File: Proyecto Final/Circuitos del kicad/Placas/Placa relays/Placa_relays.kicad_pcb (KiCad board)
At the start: 2 copper layers, 266.2 x 179.3 mm, 47 parts, among them J1 12v, J4 Conn_01x08, J5 Conn_01x08, J6 Conn_01x06, Q1 PN2222A, Q2 PN2222A, Q3 PN2222A, SW1 SW_Push, SW2 SW_Push, SW3 SW_Push, SW4 SW_Push, U1 LM7805, U2 ESP-12E, U3 ATmega328P-P, U4 LM1117-3.3, U5 BOB-12009, Y1 16MHz

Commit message: Cambios placa relays
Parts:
- removed C1, C2: 20pF, Capacitor_THT:C_Disc_D5.0mm_W2.5mm_P5.00mm
- removed C3: 330nF, Capacitor_THT:C_Disc_D5.0mm_W2.5mm_P5.00mm
- removed C4, C5: 100nF, Capacitor_THT:C_Disc_D5.0mm_W2.5mm_P5.00mm
- removed C6: 10uF, Capacitor_THT:C_Disc_D5.0mm_W2.5mm_P5.00mm
- removed Encoder/puls-arduino1: Conn_02x06_Odd_Even, ENCODER+PULS:ENCODER+PULS_arduino
- removed Encoder/puls2: Conn_02x06_Odd_Even, ENCODER+PULS:ENCODER+PULS
- removed Encoder1: Conn_01x05, Connector_PinHeader_2.54mm:PinHeader_1x05_P2.54mm_Vertical
- removed J4, J5: Conn_01x08, Connector_PinHeader_2.54mm:PinHeader_1x08_P2.54mm_Vertical
- removed J6: Conn_01x06, Connector_PinHeader_2.54mm:PinHeader_1x06_P2.54mm_Vertical
- removed R7, R8: 10k, Resistor_THT:R_Axial_DIN0204_L3.6mm_D1.6mm_P5.08mm_Horizontal
- removed RTC+LCD1: Conn_02x04_Odd_Even, Connector_PinHeader_2.54mm:PinHeader_2x04_P2.54mm_Vertical
- removed Relay+DS18B20+LVL_SENS1: Conn_02x05_Odd_Even_1, RELAY+DS18B20+LVLSENS:RELAY+DS18B20+LVLSENS
- removed Relay1: Conn_02x05_Odd_Even, RELAY+DS18B20+LVLSENS:ENCODER+PULS_PLACA_SALIDAS
- removed SW1, SW2, SW3, SW4: SW_Push, Button_Switch_THT:SW_PUSH-12mm
- removed U1: LM7805, Package_TO_SOT_THT:TO-220-3_Vertical
- removed U2: ESP-12E, ESP8266-12E_ESP-12E:XCVR_ESP8266-12E_ESP-12E
- removed U3: ATmega328P-P, Package_DIP:DIP-28_W7.62mm
- removed U4: LM1117-3.3, Package_TO_SOT_SMD:SOT-223
- removed U5: BOB-12009, Conversor_logico_nivel:CONV_BOB-12009
- removed Y1: 16MHz, Crystal:Crystal_HC49-4H_Vertical
- added D4: LED, LED_THT:LED_D5.0mm, F.Cu at (147.7, 120.2)
- added D5: LED, LED_THT:LED_D5.0mm, F.Cu at (148.0, 93.7)
- added D6: LED, LED_THT:LED_D5.0mm, F.Cu at (148.2, 67.4)
- J1: value 12v -> Conn_02x05_Odd_Even; footprint TerminalBlock:TerminalBlock_bornier-2_P5.08mm -> Connector_IDC:IDC-Header_2x05_P2.54mm_Vertical
- R1: value 4.7k -> 470
- R5, R6: value 10k -> 470
- moved Salidas_sensores1 104.1 mm to (187.3, 67.2)
- moved D3 102.0 mm to (148.5, 75.4)
- moved R5 101.9 mm to (137.2, 91.5), turned to 0 degrees
- moved Salida-3 100.1 mm to (187.3, 101.0)
- moved D2 99.6 mm to (148.6, 86.7)
- moved R3 99.4 mm to (125.8, 77.8)
- moved Q1 99.3 mm to (130.6, 76.5)
- moved Salida-2 98.8 mm to (187.3, 114.1)
- moved Relay-1 97.7 mm to (154.5, 125.6)
- moved Relay-2 97.7 mm to (154.5, 97.4)
- moved Relay-3 97.7 mm to (154.6, 69.2)
- moved Salida-1 97.7 mm to (187.3, 127.1)
- moved R4 97.2 mm to (125.7, 86.3)
- moved D1 96.3 mm to (148.5, 99.3)
- moved R2 95.5 mm to (126.1, 95.2)
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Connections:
- J1 pad 2: +12V -> GND
- R1 pad 1: Net-(R1-Pad1) -> Net-(D1-Pad2)
- R1 pad 2: +5V -> Net-(D4-Pad2)
- R5 pad 1: Net-(Encoder/puls2-Pad3) -> Net-(D2-Pad2)
- R5 pad 2: +5V -> Net-(D5-Pad2)
- R6 pad 1: Net-(Encoder/puls2-Pad5) -> Net-(D3-Pad2)
- R6 pad 2: +5V -> Net-(D6-Pad2)
- Salidas_sensores1 pad 2: Net-(Relay1-Pad7) -> Net-(Salidas_sensores1-Pad2)
- Salidas_sensores1 pad 3: Net-(Relay1-Pad5) -> Net-(Salidas_sensores1-Pad3)
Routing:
- net +5V: track 560.4 -> 132.0 mm
- net GND: track 250.2 -> 0.02 mm, vias 7 -> 0
- net Net-(Encoder/puls2-Pad4): track 158.0 -> 0.00 mm
- net Net-(Encoder/puls2-Pad6): track 152.8 -> 0.00 mm
- net Net-(Encoder/puls2-Pad8): track 148.0 -> 0.00 mm
- net Net-(Encoder/puls-arduino1-Pad7): track 147.8 -> 0.00 mm, vias 2 -> 0
- net Net-(Relay1-Pad7): track 139.5 -> 0.00 mm
- net Net-(Relay1-Pad5): track 135.8 -> 0.00 mm
- net Net-(Salidas_sensores1-Pad2): track 0.00 -> 127.7 mm
- net Net-(Salidas_sensores1-Pad3): track 0.00 -> 125.3 mm
- net Net-(J4-Pad1): track 99.4 -> 0.00 mm, vias 1 -> 0
- net Net-(Encoder/puls2-Pad9): track 48.4 -> 0.00 mm
- net Net-(Encoder/puls2-Pad3): track 47.5 -> 0.00 mm
- net Net-(C6-Pad1): track 46.7 -> 0.00 mm, vias 1 -> 0
- net Net-(Encoder/puls-arduino1-Pad5): track 44.2 -> 0.00 mm
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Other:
- board size 266.2 x 179.3 mm -> 89.9 x 85.7 mm
- board text added: "-"
- board text added: "L"
- board text added: "T"

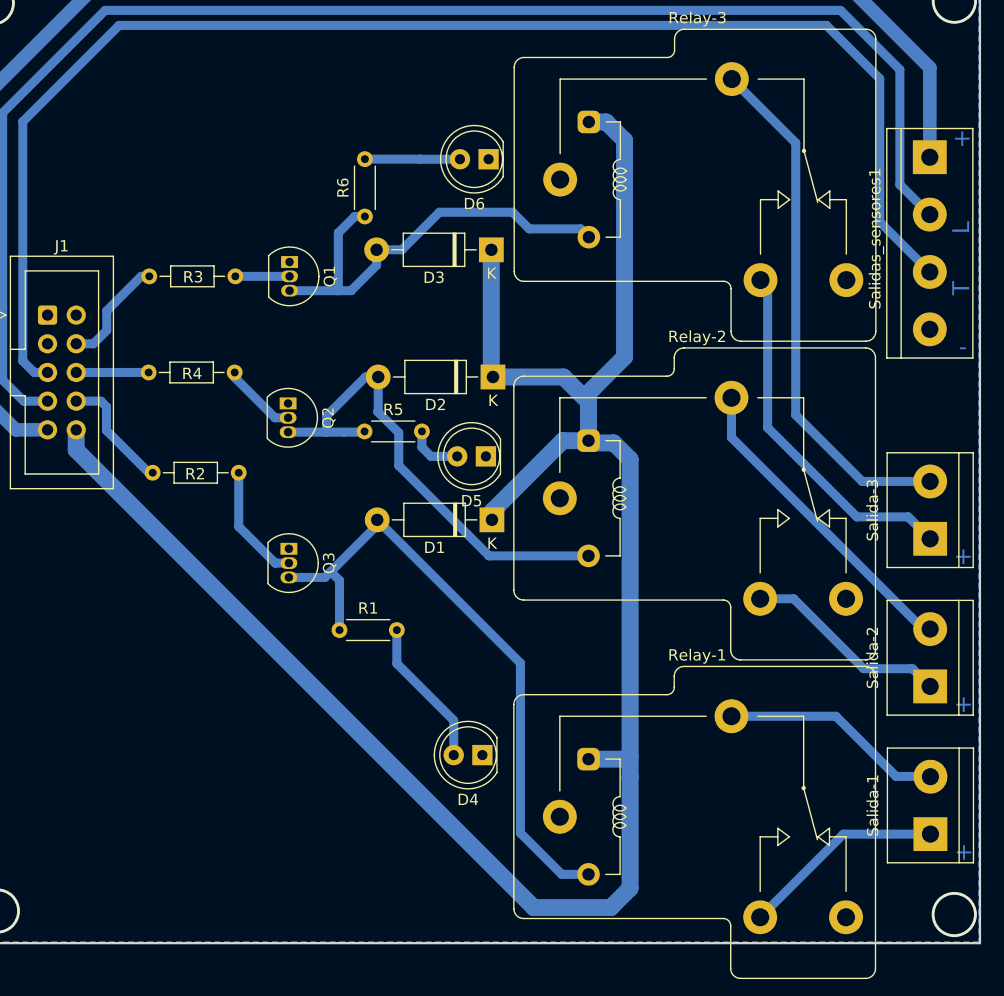
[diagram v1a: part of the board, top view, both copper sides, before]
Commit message: Agregado placa todo en uno
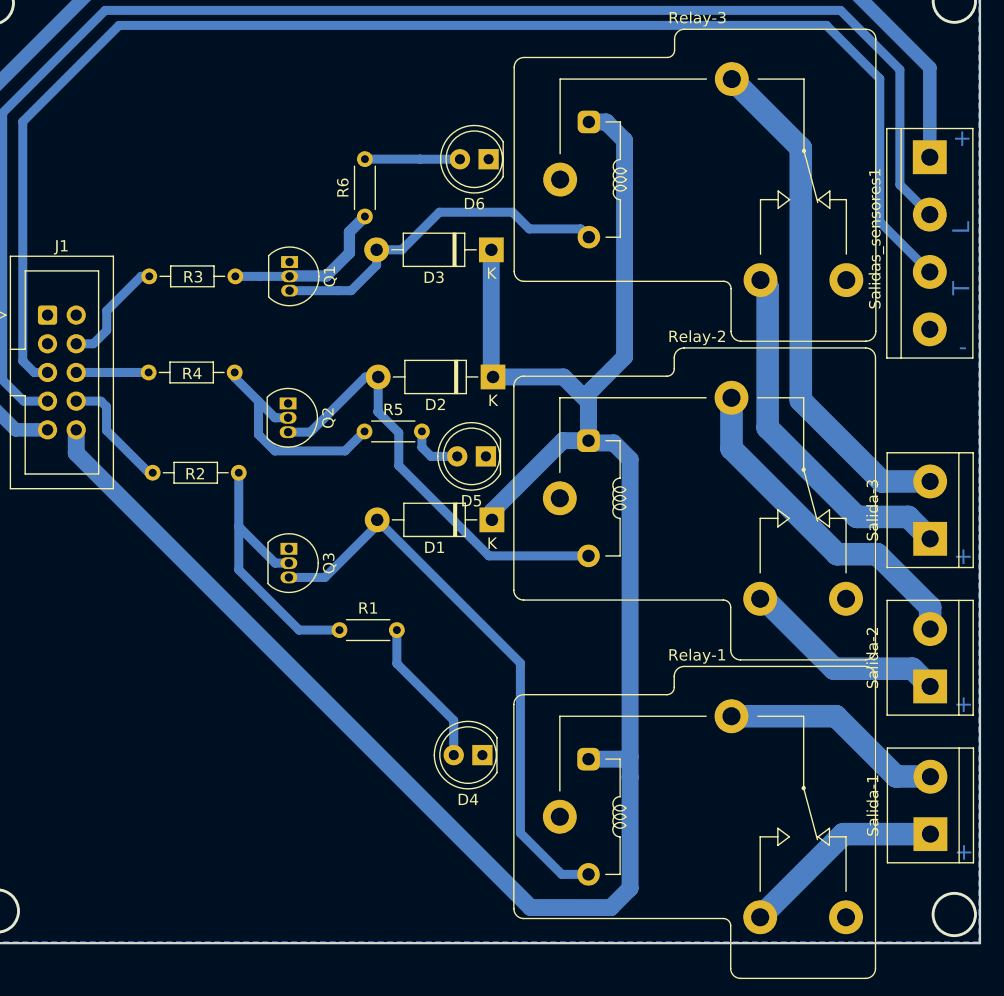
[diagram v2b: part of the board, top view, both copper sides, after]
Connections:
- R1 pad 1: Net-(D1-Pad2) -> Net-(Q3-Pad2)
- R5 pad 1: Net-(D2-Pad2) -> Net-(Q2-Pad2)
- R6 pad 1: Net-(D3-Pad2) -> Net-(Q1-Pad2)
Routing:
- net Net-(Q3-Pad2): track 10.5 -> 25.5 mm
- net Net-(Q2-Pad2): track 6.65 -> 20.3 mm
- net Net-(Q1-Pad2): track 4.80 -> 14.8 mm
- net Net-(D3-Pad2): track 39.2 -> 31.1 mm
- net Net-(D1-Pad2): track 56.2 -> 50.7 mm
- net Net-(D2-Pad2): track 43.0 -> 38.7 mm
- net Net-(Relay-2-Pad11A): track 28.1 -> 29.8 mm
- net Net-(Relay-3-Pad11A): track 46.4 -> 45.4 mm
